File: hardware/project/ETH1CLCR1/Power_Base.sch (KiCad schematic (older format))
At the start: 16 parts, among them Q601 IRFR5410, U601 LM1117IMP-3.3/NOPB, U602 TSR1-2450, U603 MAX5902

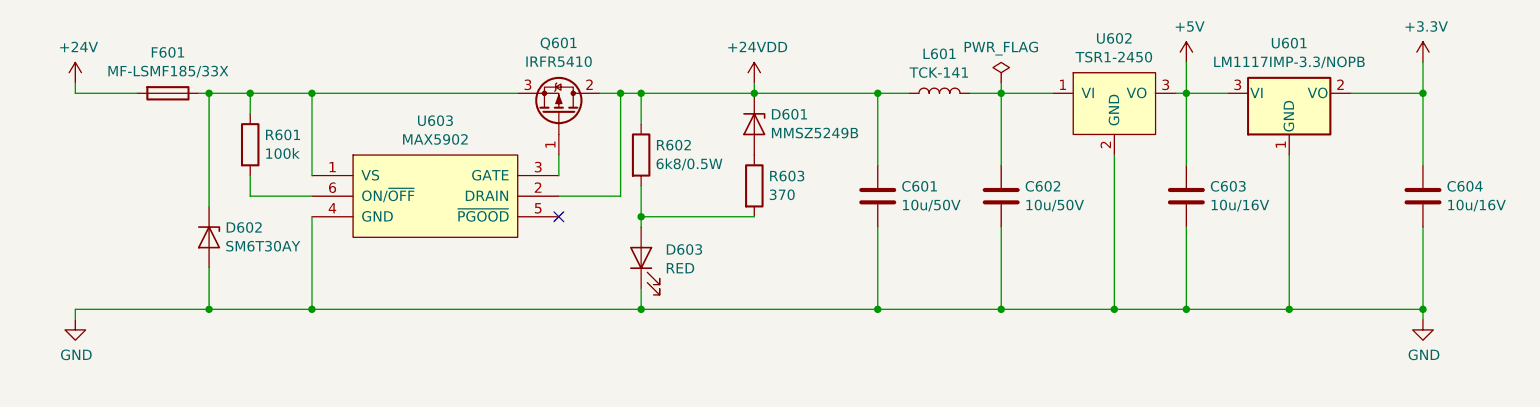
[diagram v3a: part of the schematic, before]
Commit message: Footprint asigment (not finished).
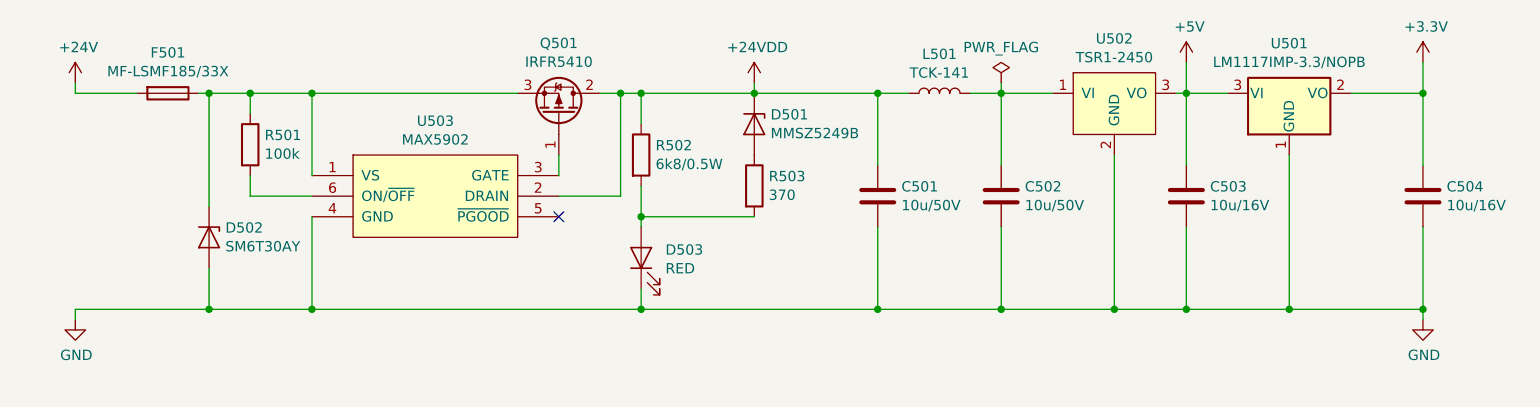
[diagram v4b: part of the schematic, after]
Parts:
- renumbered C601 to C501, C602 to C502, C603 to C503, C604 to C504, D601 to D501, D602 to D502, D603 to D503, F601 to F501, L601 to L501, Q601 to Q501, R601 to R501, R602 to R502, R603 to R503, U601 to U501, U602 to U502, U603 to U503
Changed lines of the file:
@@
 $Descr A4 11693 8268
 encoding utf-8
-Sheet 7 16
+Sheet 5 16
 Title ""
 Date ""
@@
 	6250 3900 6250 4300
 $Comp
-L power:GND #PWR0605
+L power:GND #PWR0505
 U 1 1 5D6E9D93
 P 2350 4350
-F 0 "#PWR0605" H 2350 4100 50  0001 C CNN
+F 0 "#PWR0505" H 2350 4100 50  0001 C CNN
 F 1 "GND" H 2355 4177 50  0000 C CNN
 F 2 "" H 2350 4350 50  0001 C CNN
@@
 	3000 3800 3000 3250
 $Comp
-L Device:D_Zener D602
+L Device:D_Zener D502
 U 1 1 5D70DE79
 P 3000 3950
-F 0 "D602" V 2954 4029 50  0000 L CNN
+F 0 "D502" V 2954 4029 50  0000 L CNN
 F 1 "SM6T30AY" V 3045 4029 50  0000 L CNN
 F 2 "ETH1CLCR1:DO_214AA_REV" H 3000 3950 50  0001 C CNN
@@
 Connection ~ 5100 3850
 $Comp
-L Device:D_Zener D601
+L Device:D_Zener D501
 U 1 1 5D6DFA8C
 P 5650 3400
-F 0 "D601" V 5604 3479 50  0000 L CNN
+F 0 "D501" V 5604 3479 50  0000 L CNN
 F 1 "MMSZ5249B" V 5695 3479 50  0000 L CNN
 F 2 "Diode_SMD:D_SOD-123" H 5650 3400 50  0001 C CNN
@@
 	5100 3250 5100 3400
 $Comp
-L Device:R R603
+L Device:R R503
 U 1 1 5D6D8193
 P 5650 3700
-F 0 "R603" H 5720 3746 50  0000 L CNN
+F 0 "R503" H 5720 3746 50  0000 L CNN
 F 1 "370" H 5720 3655 50  0000 L CNN
 F 2 "Resistor_SMD:R_0603_1608Metric_Pad1.05x0.95mm_HandSolder" V 5580 3700 50  0001 C CNN
@@
 $EndComp
 $Comp
-L Device:R R602
+L Device:R R502
 U 1 1 5D6D7B1E
 P 5100 3550
-F 0 "R602" H 5170 3596 50  0000 L CNN
+F 0 "R502" H 5170 3596 50  0000 L CNN
 F 1 "6k8/0.5W" H 5170 3505 50  0000 L CNN
 F 2 "Resistor_SMD:R_0805_2012Metric_Pad1.15x1.40mm_HandSolder" V 5030 3550 50  0001 C CNN
@@
 $EndComp
 $Comp
-L Device:LED D603
+L Device:LED D503
 U 1 1 5D6D7414
 P 5100 4050
-F 0 "D603" V 5139 3932 50  0000 R CNN
+F 0 "D503" V 5139 3932 50  0000 R CNN
 F 1 "RED" V 5048 3932 50  0000 R CNN
 F 2 "LED_SMD:LED_0603_1608Metric_Pad1.05x0.95mm_HandSolder" H 5100 4050 50  0001 C CNN
@@
 	6250 3600 6250 3250
 $Comp
-L Device:C C601
+L Device:C C501
 U 1 1 5D6CEB9C
 P 6250 3750
-F 0 "C601" H 6365 3796 50  0000 L CNN
+F 0 "C501" H 6365 3796 50  0000 L CNN
 F 1 "10u/50V" H 6365 3705 50  0000 L CNN
 F 2 "Capacitor_SMD:C_1206_3216Metric_Pad1.42x1.75mm_HandSolder" H 6288 3600 50  0001 C CNN
@@
 	2650 3250 2350 3250
 $Comp
-L Device:Fuse F601
+L Device:Fuse F501
 U 1 1 5D5D8684
 P 2800 3250
-F 0 "F601" V 2603 3250 50  0000 C CNN
+F 0 "F501" V 2603 3250 50  0000 C CNN
 F 1 "MF-LSMF185/33X" V 2694 3250 50  0000 C CNN
 F 2 "ETH1CLCR1:Fuse_SMD2920" V 2730 3250 50  0001 C CNN
@@
 $EndComp
 $Comp
-L power:+24V #PWR0603
+L power:+24V #PWR0503
 U 1 1 5D7B3705
 P 2350 3200
-F 0 "#PWR0603" H 2350 3050 50  0001 C CNN
+F 0 "#PWR0503" H 2350 3050 50  0001 C CNN
 F 1 "+24V" H 2365 3373 50  0000 C CNN
 F 2 "" H 2350 3200 50  0001 C CNN
@@
 	3000 3250 3200 3250
 $Comp
-L ETH1CLCR1:MAX5902 U603
+L ETH1CLCR1:MAX5902 U503
 U 1 1 5D6EBA14
 P 4100 3750
-F 0 "U603" H 4100 4115 50  0000 C CNN
+F 0 "U503" H 4100 4115 50  0000 C CNN
 F 1 "MAX5902" H 4100 4024 50  0000 C CNN
 F 2 "Package_TO_SOT_SMD:SOT-23-6_Handsoldering" H 4100 3750 60  0001 C CNN
@@
 $EndComp
 $Comp
-L Device:Q_PMOS_GDS Q601
+L Device:Q_PMOS_GDS Q501
 U 1 1 5D6F32E4
 P 4700 3350
-F 0 "Q601" V 5043 3350 50  0000 C CNN
+F 0 "Q501" V 5043 3350 50  0000 C CNN
 F 1 "IRFR5410" V 4952 3350 50  0000 C CNN
 F 2 "ETH1CLCR1:TO-252-2_Rectifier" H 4900 3450 50  0001 C CNN
@@
 	3500 3650 3500 3250
 $Comp
-L Device:R R601
+L Device:R R501
 U 1 1 5D709595
 P 3200 3500
-F 0 "R601" H 3270 3546 50  0000 L CNN
+F 0 "R501" H 3270 3546 50  0000 L CNN
 F 1 "100k" H 3270 3455 50  0000 L CNN
 F 2 "Resistor_SMD:R_0603_1608Metric_Pad1.05x0.95mm_HandSolder" V 3130 3500 50  0001 C CNN
@@
 	7400 3550 7400 4300
 $Comp
-L Device:L L601
+L Device:L L501
 U 1 1 5DA651AB
 P 6550 3250
-F 0 "L601" V 6740 3250 50  0000 C CNN
+F 0 "L501" V 6740 3250 50  0000 C CNN
 F 1 "TCK-141" V 6649 3250 50  0000 C CNN
 F 2 "ETH1CLCR1:TCK-141" H 6550 3250 50  0001 C CNN
@@
 $EndComp
 $Comp
-L Device:C C602
+L Device:C C502
 U 1 1 5DA6571D
 P 6850 3750
-F 0 "C602" H 6965 3796 50  0000 L CNN
+F 0 "C502" H 6965 3796 50  0000 L CNN
 F 1 "10u/50V" H 6965 3705 50  0000 L CNN
 F 2 "Capacitor_SMD:C_1206_3216Metric_Pad1.42x1.75mm_HandSolder" H 6888 3600 50  0001 C CNN
@@
 Connection ~ 5100 4300
 $Comp
-L ETH1CLCR1:+24VDD #PWR0604
+L ETH1CLCR1:+24VDD #PWR0504
 U 1 1 5DA9B429
 P 5650 3200
-F 0 "#PWR0604" H 5650 3050 50  0001 C CNN
+F 0 "#PWR0504" H 5650 3050 50  0001 C CNN
 F 1 "+24VDD" H 5665 3373 50  0000 C CNN
 F 2 "" H 5650 3200 50  0001 C CNN
@@
 	5650 3200 5650 3250
 $Comp
-L ETH1CLCR1:TSR1-2450 U602
+L ETH1CLCR1:TSR1-2450 U502
 U 1 1 5DAB8D35
 P 7400 3300
-F 0 "U602" H 7400 3615 50  0000 C CNN
+F 0 "U502" H 7400 3615 50  0000 C CNN
 F 1 "TSR1-2450" H 7400 3524 50  0000 C CNN
 F 2 "ETH1CLCR1:TSR1" H 7400 3300 50  0001 C CNN
@@
 	7750 3100 7750 3250
 $Comp
-L power:+5V #PWR0601
+L power:+5V #PWR0501
 U 1 1 5DD09470
 P 7750 3100
-F 0 "#PWR0601" H 7750 2950 50  0001 C CNN
+F 0 "#PWR0501" H 7750 2950 50  0001 C CNN
 F 1 "+5V" H 7765 3273 50  0000 C CNN
 F 2 "" H 7750 3100 50  0001 C CNN
@@
 	8900 3100 8900 3250
 $Comp
-L power:+3.3V #PWR0602
+L power:+3.3V #PWR0502
 U 1 1 5DA96AF7
 P 8900 3100
-F 0 "#PWR0602" H 8900 2950 50  0001 C CNN
+F 0 "#PWR0502" H 8900 2950 50  0001 C CNN
 F 1 "+3.3V" H 8915 3273 50  0000 C CNN
 F 2 "" H 8900 3100 50  0001 C CNN
@@
 	8900 3600 8900 3250
 $Comp
-L Device:C C604
+L Device:C C504
 U 1 1 5DAAAE75
 P 8900 3750
-F 0 "C604" H 9015 3796 50  0000 L CNN
+F 0 "C504" H 9015 3796 50  0000 L CNN
 F 1 "10u/16V" H 9015 3705 50  0000 L CNN
 F 2 "Capacitor_SMD:C_1206_3216Metric_Pad1.42x1.75mm_HandSolder" H 8938 3600 50  0001 C CNN
@@
 $EndComp
 $Comp
-L Regulator_Linear:LM1117-3.3 U601
+L Regulator_Linear:LM1117-3.3 U501
 U 1 1 5DAAA77C
 P 8250 3250
-F 0 "U601" H 8250 3492 50  0000 C CNN
+F 0 "U501" H 8250 3492 50  0000 C CNN
 F 1 "LM1117IMP-3.3/NOPB" H 8250 3401 50  0000 C CNN
 F 2 "Package_TO_SOT_SMD:SOT-223-3_TabPin2" H 8250 3250 50  0001 C CNN
@@
 $EndComp
 $Comp
-L power:GND #PWR0606
+L power:GND #PWR0506
 U 1 1 5DAA429A
 P 8900 4350
-F 0 "#PWR0606" H 8900 4100 50  0001 C CNN
+F 0 "#PWR0506" H 8900 4100 50  0001 C CNN
 F 1 "GND" H 8905 4177 50  0000 C CNN
 F 2 "" H 8900 4350 50  0001 C CNN
@@
 	7750 3900 7750 4300
 $Comp
-L Device:C C603
+L Device:C C503
 U 1 1 5DA5FEE0
 P 7750 3750
-F 0 "C603" H 7865 3796 50  0000 L CNN
+F 0 "C503" H 7865 3796 50  0000 L CNN
 F 1 "10u/16V" H 7865 3705 50  0000 L CNN
 F 2 "Capacitor_SMD:C_1206_3216Metric_Pad1.42x1.75mm_HandSolder" H 7788 3600 50  0001 C CNN
@@
 	6850 3250 7100 3250
 $Comp
-L power:PWR_FLAG #FLG0601
+L power:PWR_FLAG #FLG0501
 U 1 1 5E5270F4
 P 6850 3200
-F 0 "#FLG0601" H 6850 3275 50  0001 C CNN
+F 0 "#FLG0501" H 6850 3275 50  0001 C CNN
 F 1 "PWR_FLAG" H 6850 3373 50  0000 C CNN
 F 2 "" H 6850 3200 50  0001 C CNN
@@
 	6850 3200 6850 3250
 $Comp
-L power:PWR_FLAG #FLG0602
+L power:PWR_FLAG #FLG0502
 U 1 1 5DDE91B3
 P 850 7350
-F 0 "#FLG0602" H 850 7425 50  0001 C CNN
+F 0 "#FLG0502" H 850 7425 50  0001 C CNN
 F 1 "PWR_FLAG" H 850 7523 50  0000 C CNN
 F 2 "" H 850 7350 50  0001 C CNN
@@
 $EndComp
 $Comp
-L power:+24V #PWR0607
+L power:+24V #PWR0507
 U 1 1 5DDE9577
 P 850 7350
-F 0 "#PWR0607" H 850 7200 50  0001 C CNN
+F 0 "#PWR0507" H 850 7200 50  0001 C CNN
 F 1 "+24V" H 865 7523 50  0000 C CNN
 F 2 "" H 850 7350 50  0001 C CNN
@@
 $EndComp
 $Comp
-L power:PWR_FLAG #FLG0603
+L power:PWR_FLAG #FLG0503
 U 1 1 5DDF63B9
 P 1300 7350
-F 0 "#FLG0603" H 1300 7425 50  0001 C CNN
+F 0 "#FLG0503" H 1300 7425 50  0001 C CNN
 F 1 "PWR_FLAG" H 1300 7523 50  0000 C CNN
 F 2 "" H 1300 7350 50  0001 C CNN
@@
 $EndComp
 $Comp
-L power:GND #PWR0608
+L power:GND #PWR0508
 U 1 1 5DDF6902
 P 1300 7350
-F 0 "#PWR0608" H 1300 7100 50  0001 C CNN
+F 0 "#PWR0508" H 1300 7100 50  0001 C CNN
 F 1 "GND" H 1305 7177 50  0000 C CNN
 F 2 "" H 1300 7350 50  0001 C CNN
@@
 $EndComp
 $Comp
-L power:PWR_FLAG #FLG0604
+L power:PWR_FLAG #FLG0504
 U 1 1 5DDFBB5F
 P 1750 7350
-F 0 "#FLG0604" H 1750 7425 50  0001 C CNN
+F 0 "#FLG0504" H 1750 7425 50  0001 C CNN
 F 1 "PWR_FLAG" H 1750 7523 50  0000 C CNN
 F 2 "" H 1750 7350 50  0001 C CNN
@@
 $EndComp
 $Comp
-L ETH1CLCR1:+24VDD #PWR0609
+L ETH1CLCR1:+24VDD #PWR0509
 U 1 1 5DDFC0E6
 P 1750 7350
-F 0 "#PWR0609" H 1750 7200 50  0001 C CNN
+F 0 "#PWR0509" H 1750 7200 50  0001 C CNN
 F 1 "+24VDD" H 1765 7523 50  0000 C CNN
 F 2 "" H 1750 7350 50  0001 C CNN

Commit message: Redesinged ADC schematic.
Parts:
- renumbered D502 to D501, D503 to D502, D501 to D503, U503 to U501, U501 to U503
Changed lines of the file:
@@
 	3000 3800 3000 3250
 $Comp
-L Device:D_Zener D502
+L Device:D_Zener D501
 U 1 1 5D70DE79
 P 3000 3950
-F 0 "D502" V 2954 4029 50  0000 L CNN
+F 0 "D501" V 2954 4029 50  0000 L CNN
 F 1 "SM6T30AY" V 3045 4029 50  0000 L CNN
 F 2 "ETH1CLCR1:DO_214AA_REV" H 3000 3950 50  0001 C CNN
@@
 Connection ~ 5100 3850
 $Comp
-L Device:D_Zener D501
+L Device:D_Zener D503
 U 1 1 5D6DFA8C
 P 5650 3400
-F 0 "D501" V 5604 3479 50  0000 L CNN
+F 0 "D503" V 5604 3479 50  0000 L CNN
 F 1 "MMSZ5249B" V 5695 3479 50  0000 L CNN
 F 2 "Diode_SMD:D_SOD-123" H 5650 3400 50  0001 C CNN
@@
 $EndComp
 $Comp
-L Device:LED D503
+L Device:LED D502
 U 1 1 5D6D7414
 P 5100 4050
-F 0 "D503" V 5139 3932 50  0000 R CNN
+F 0 "D502" V 5139 3932 50  0000 R CNN
 F 1 "RED" V 5048 3932 50  0000 R CNN
 F 2 "LED_SMD:LED_0603_1608Metric_Pad1.05x0.95mm_HandSolder" H 5100 4050 50  0001 C CNN
@@
 $EndComp
 $Comp
-L power:+24V #PWR0503
+L power:+24V #PWR0504
 U 1 1 5D7B3705
 P 2350 3200
-F 0 "#PWR0503" H 2350 3050 50  0001 C CNN
+F 0 "#PWR0504" H 2350 3050 50  0001 C CNN
 F 1 "+24V" H 2365 3373 50  0000 C CNN
 F 2 "" H 2350 3200 50  0001 C CNN
@@
 	3000 3250 3200 3250
 $Comp
-L ETH1CLCR1:MAX5902 U503
+L ETH1CLCR1:MAX5902 U501
 U 1 1 5D6EBA14
 P 4100 3750
-F 0 "U503" H 4100 4115 50  0000 C CNN
+F 0 "U501" H 4100 4115 50  0000 C CNN
 F 1 "MAX5902" H 4100 4024 50  0000 C CNN
 F 2 "Package_TO_SOT_SMD:SOT-23-6_Handsoldering" H 4100 3750 60  0001 C CNN
@@
 Connection ~ 5100 4300
 $Comp
-L ETH1CLCR1:+24VDD #PWR0504
+L ETH1CLCR1:+24VDD #PWR0506
 U 1 1 5DA9B429
 P 5650 3200
-F 0 "#PWR0504" H 5650 3050 50  0001 C CNN
+F 0 "#PWR0506" H 5650 3050 50  0001 C CNN
 F 1 "+24VDD" H 5665 3373 50  0000 C CNN
 F 2 "" H 5650 3200 50  0001 C CNN
@@
 	7750 3100 7750 3250
 $Comp
-L power:+5V #PWR0501
+L power:+5V #PWR0507
 U 1 1 5DD09470
 P 7750 3100
-F 0 "#PWR0501" H 7750 2950 50  0001 C CNN
+F 0 "#PWR0507" H 7750 2950 50  0001 C CNN
 F 1 "+5V" H 7765 3273 50  0000 C CNN
 F 2 "" H 7750 3100 50  0001 C CNN
@@
 	8900 3100 8900 3250
 $Comp
-L power:+3.3V #PWR0502
+L power:+3.3V #PWR0508
 U 1 1 5DA96AF7
 P 8900 3100
-F 0 "#PWR0502" H 8900 2950 50  0001 C CNN
+F 0 "#PWR0508" H 8900 2950 50  0001 C CNN
 F 1 "+3.3V" H 8915 3273 50  0000 C CNN
 F 2 "" H 8900 3100 50  0001 C CNN
@@
 $EndComp
 $Comp
-L Regulator_Linear:LM1117-3.3 U501
+L Regulator_Linear:LM1117-3.3 U503
 U 1 1 5DAAA77C
 P 8250 3250
-F 0 "U501" H 8250 3492 50  0000 C CNN
+F 0 "U503" H 8250 3492 50  0000 C CNN
 F 1 "LM1117IMP-3.3/NOPB" H 8250 3401 50  0000 C CNN
 F 2 "Package_TO_SOT_SMD:SOT-223-3_TabPin2" H 8250 3250 50  0001 C CNN
@@
 $EndComp
 $Comp
-L power:GND #PWR0506
+L power:GND #PWR0509
 U 1 1 5DAA429A
 P 8900 4350
-F 0 "#PWR0506" H 8900 4100 50  0001 C CNN
+F 0 "#PWR0509" H 8900 4100 50  0001 C CNN
 F 1 "GND" H 8905 4177 50  0000 C CNN
 F 2 "" H 8900 4350 50  0001 C CNN
@@
 	6850 3250 7100 3250
 $Comp
-L power:PWR_FLAG #FLG0501
+L power:PWR_FLAG #FLG0504
 U 1 1 5E5270F4
 P 6850 3200
-F 0 "#FLG0501" H 6850 3275 50  0001 C CNN
+F 0 "#FLG0504" H 6850 3275 50  0001 C CNN
 F 1 "PWR_FLAG" H 6850 3373 50  0000 C CNN
 F 2 "" H 6850 3200 50  0001 C CNN
@@
 	6850 3200 6850 3250
 $Comp
-L power:PWR_FLAG #FLG0502
+L power:PWR_FLAG #FLG0501
 U 1 1 5DDE91B3
 P 850 7350
-F 0 "#FLG0502" H 850 7425 50  0001 C CNN
+F 0 "#FLG0501" H 850 7425 50  0001 C CNN
 F 1 "PWR_FLAG" H 850 7523 50  0000 C CNN
 F 2 "" H 850 7350 50  0001 C CNN
@@
 $EndComp
 $Comp
-L power:+24V #PWR0507
+L power:+24V #PWR0501
 U 1 1 5DDE9577
 P 850 7350
-F 0 "#PWR0507" H 850 7200 50  0001 C CNN
+F 0 "#PWR0501" H 850 7200 50  0001 C CNN
 F 1 "+24V" H 865 7523 50  0000 C CNN
 F 2 "" H 850 7350 50  0001 C CNN
@@
 $EndComp
 $Comp
-L power:PWR_FLAG #FLG0503
+L power:PWR_FLAG #FLG0502
 U 1 1 5DDF63B9
 P 1300 7350
-F 0 "#FLG0503" H 1300 7425 50  0001 C CNN
+F 0 "#FLG0502" H 1300 7425 50  0001 C CNN
 F 1 "PWR_FLAG" H 1300 7523 50  0000 C CNN
 F 2 "" H 1300 7350 50  0001 C CNN
@@
 $EndComp
 $Comp
-L power:GND #PWR0508
+L power:GND #PWR0502
 U 1 1 5DDF6902
 P 1300 7350
-F 0 "#PWR0508" H 1300 7100 50  0001 C CNN
+F 0 "#PWR0502" H 1300 7100 50  0001 C CNN
 F 1 "GND" H 1305 7177 50  0000 C CNN
 F 2 "" H 1300 7350 50  0001 C CNN
@@
 $EndComp
 $Comp
-L power:PWR_FLAG #FLG0504
+L power:PWR_FLAG #FLG0503
 U 1 1 5DDFBB5F
 P 1750 7350
-F 0 "#FLG0504" H 1750 7425 50  0001 C CNN
+F 0 "#FLG0503" H 1750 7425 50  0001 C CNN
 F 1 "PWR_FLAG" H 1750 7523 50  0000 C CNN
 F 2 "" H 1750 7350 50  0001 C CNN
@@
 $EndComp
 $Comp
-L ETH1CLCR1:+24VDD #PWR0509
+L ETH1CLCR1:+24VDD #PWR0503
 U 1 1 5DDFC0E6
 P 1750 7350
-F 0 "#PWR0509" H 1750 7200 50  0001 C CNN
+F 0 "#PWR0503" H 1750 7200 50  0001 C CNN
 F 1 "+24VDD" H 1765 7523 50  0000 C CNN
 F 2 "" H 1750 7350 50  0001 C CNN
